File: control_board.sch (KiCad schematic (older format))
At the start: 4 parts

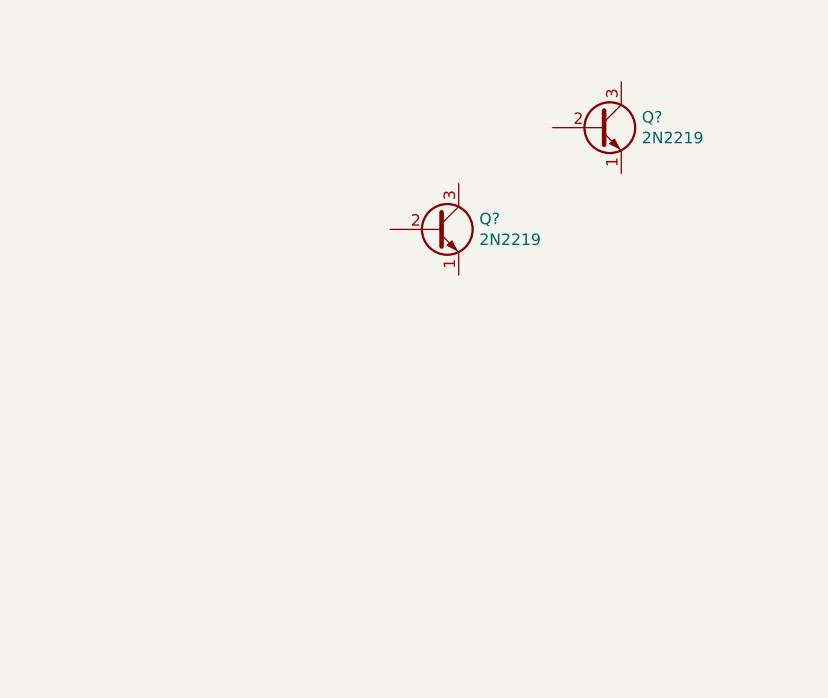
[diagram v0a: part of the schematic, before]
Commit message: Added level shifting
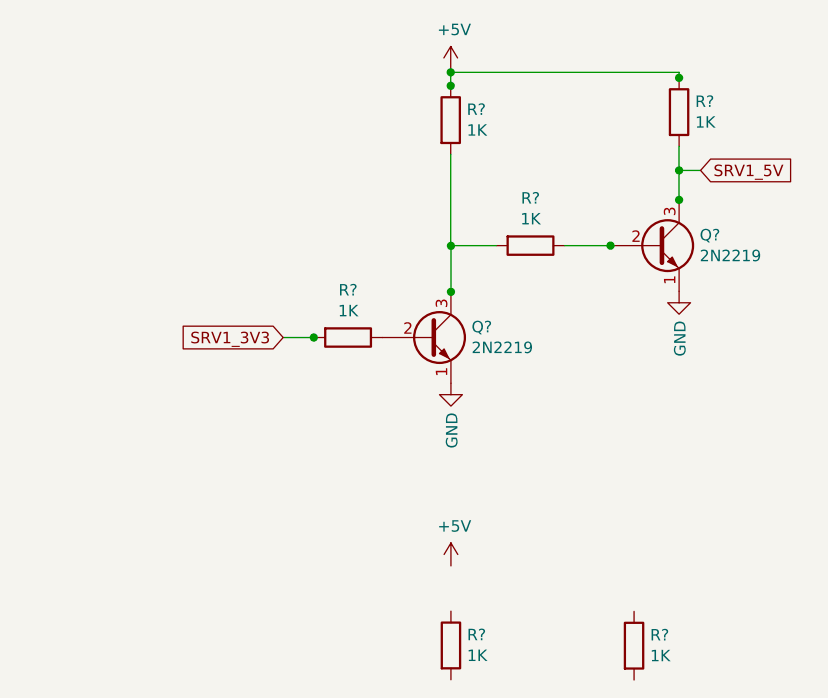
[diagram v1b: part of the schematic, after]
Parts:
- added R? (x6): 1K, symbol Device:R
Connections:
- net labels added: +5V, SRV1_3V3, SRV1_5V
- wire segments 0 -> 20
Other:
- moved on the sheet: Q?

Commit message: Routed board layout
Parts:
- added C1, C2: 10uF, Capacitor_SMD:C_0805_2012Metric, symbol Device:C
- added D1, D3, D4, D5, D6, D7, D8: LED, LED_SMD:LED_0805_2012Metric, symbol Device:LED
- added H1, H2, H3, H4, H5, H6, H7: MountingHole_Pad, MountingHole:MountingHole_3mm_Pad_Via, symbol Mechanical:MountingHole_Pad
- added J1: Conn_01x02_Female, Connector_PinHeader_2.54mm:PinHeader_1x02_P2.54mm_Vertical, symbol Connector:Conn_01x02_Female
- added J10, J15, J16: Conn_02x04_Odd_Even, Connector_PinSocket_2.54mm:PinSocket_2x04_P2.54mm_Vertical, symbol Connector_Generic:Conn_02x04_Odd_Even
- added J11: Screw_Terminal_01x02, TerminalBlock:TerminalBlock_Altech_AK300-2_P5.00mm, symbol Connector:Screw_Terminal_01x02
- added J12, J13, J14, J17, J18, J9: Conn_01x03, Connector_PinHeader_2.54mm:PinHeader_1x03_P2.54mm_Vertical, symbol Connector_Generic:Conn_01x03
- added J19: Conn_02x03_Odd_Even, Connector_PinHeader_2.54mm:PinHeader_2x03_P2.54mm_Vertical, symbol Connector_Generic:Conn_02x03_Odd_Even
- added J4, J5, J6, J7: Conn_01x01, Connector_PinSocket_2.54mm:PinSocket_1x01_P2.54mm_Vertical, symbol Connector_Generic:Conn_01x01
- added J8: Conn_01x03, Connector_PinSocket_2.54mm:PinSocket_1x03_P2.54mm_Vertical, symbol Connector_Generic:Conn_01x03
- added Q1, Q10, Q11, Q2, Q3, Q4, Q5, Q6, Q7, Q8: 2N2219, Package_TO_SOT_THT:TO-92, symbol Transistor_BJT:2N2219
- added R1, R3, R4, R5, R6, R7, R8: 220, Resistor_SMD:R_0805_2012Metric, symbol Device:R
- added R10, R11, R12, R13, R14, R16, R17, R18, R19, R20, R23, R24, R25, R26, R29, R30, R31, R32: 1K, Resistor_SMD:R_0805_2012Metric, symbol Device:R
- added R9: 1M, Resistor_SMD:R_0805_2012Metric, symbol Device:R
- added SW1, SW2, SW3, SW4: SW_Push, Button_Switch_THT:SW_PUSH_6mm, symbol Switch:SW_Push
- added TP1, TP2, TP3: TestPoint, TestPoint:TestPoint_Pad_D1.5mm, symbol Connector:TestPoint
- added U1: LM1117-3.3, Package_TO_SOT_SMD:SOT-223, symbol Regulator_Linear:LM1117-3.3
- J2, J3: renamed from J?; footprint (none) -> Connector_PinSocket_2.54mm:PinSocket_2x25_P2.54mm_Vertical
- Q12, Q9: renamed from Q?; footprint Package_TO_SOT_THT:TO-39-3 -> Package_TO_SOT_THT:TO-92
- R15, R21, R22, R27, R28, R33: renamed from R?; footprint (none) -> Resistor_SMD:R_0805_2012Metric
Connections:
- net labels added: +12V, +3.3V, DEBUG_RX, DEBUG_TX, PA_4, PD_0, PD_1, PD_2, PD_3, PD_4, PD_5, PD_6, PE_0, PE_1, PE_2, PE_3, SRV2_3V3, SRV2_5V, SRV3_3V3, SRV3_5V, SRV4_3V3, SRV4_5V, SRV5_3V3, SRV5_5V, SRV6_3V3, SRV6_5V, USART_RX, USART_TX
- wire segments 20 -> 100
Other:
- moved on the sheet: J2, J3, Q12, Q9, R15, R21, R22, R27, R28, R33

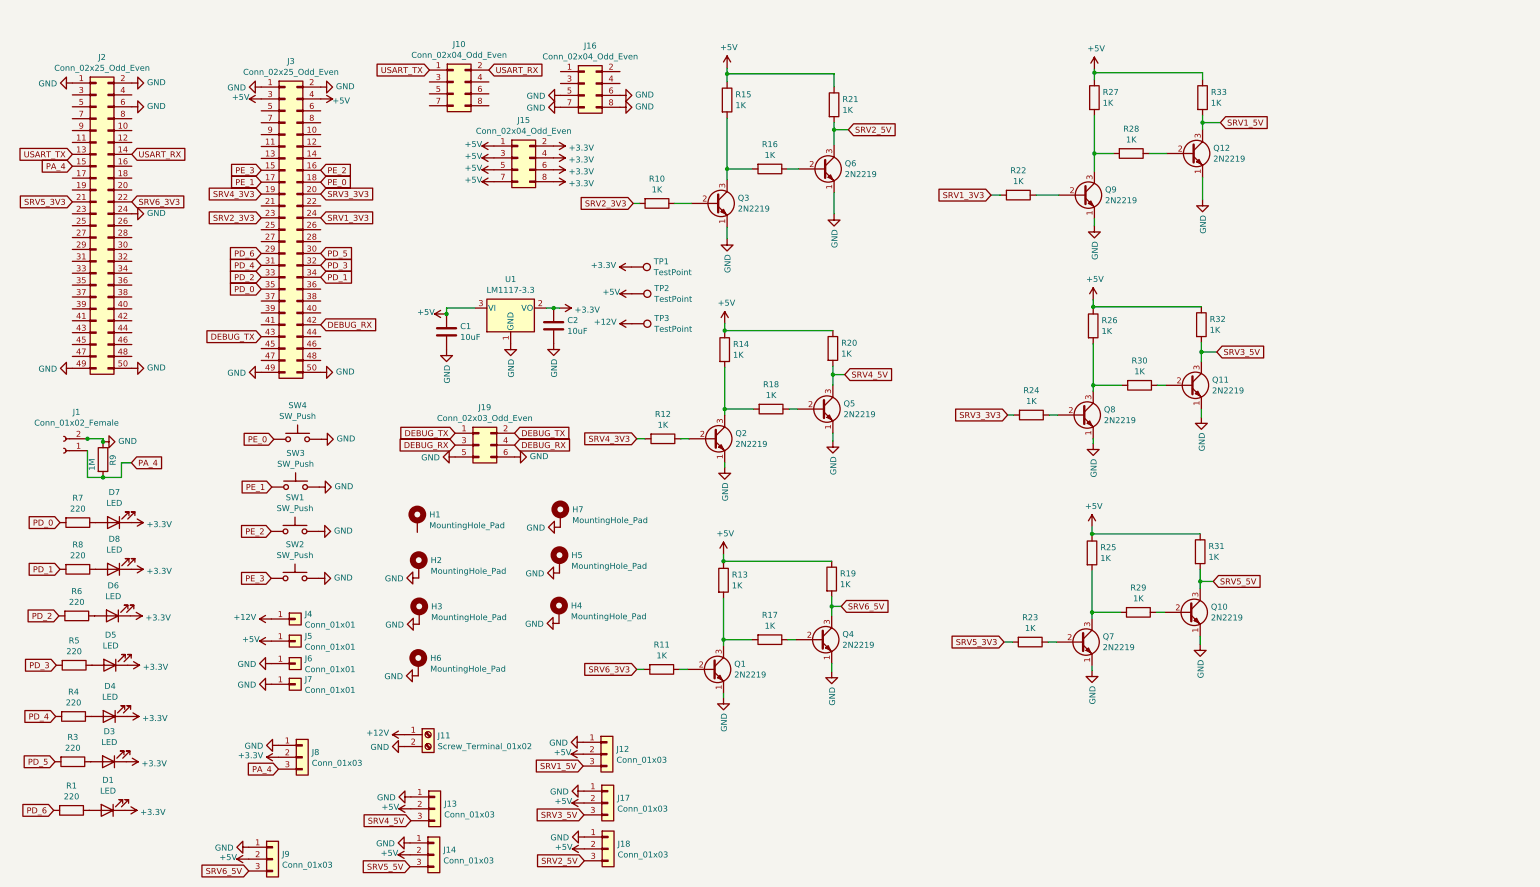
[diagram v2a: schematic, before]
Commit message: added ESP8266 circuit
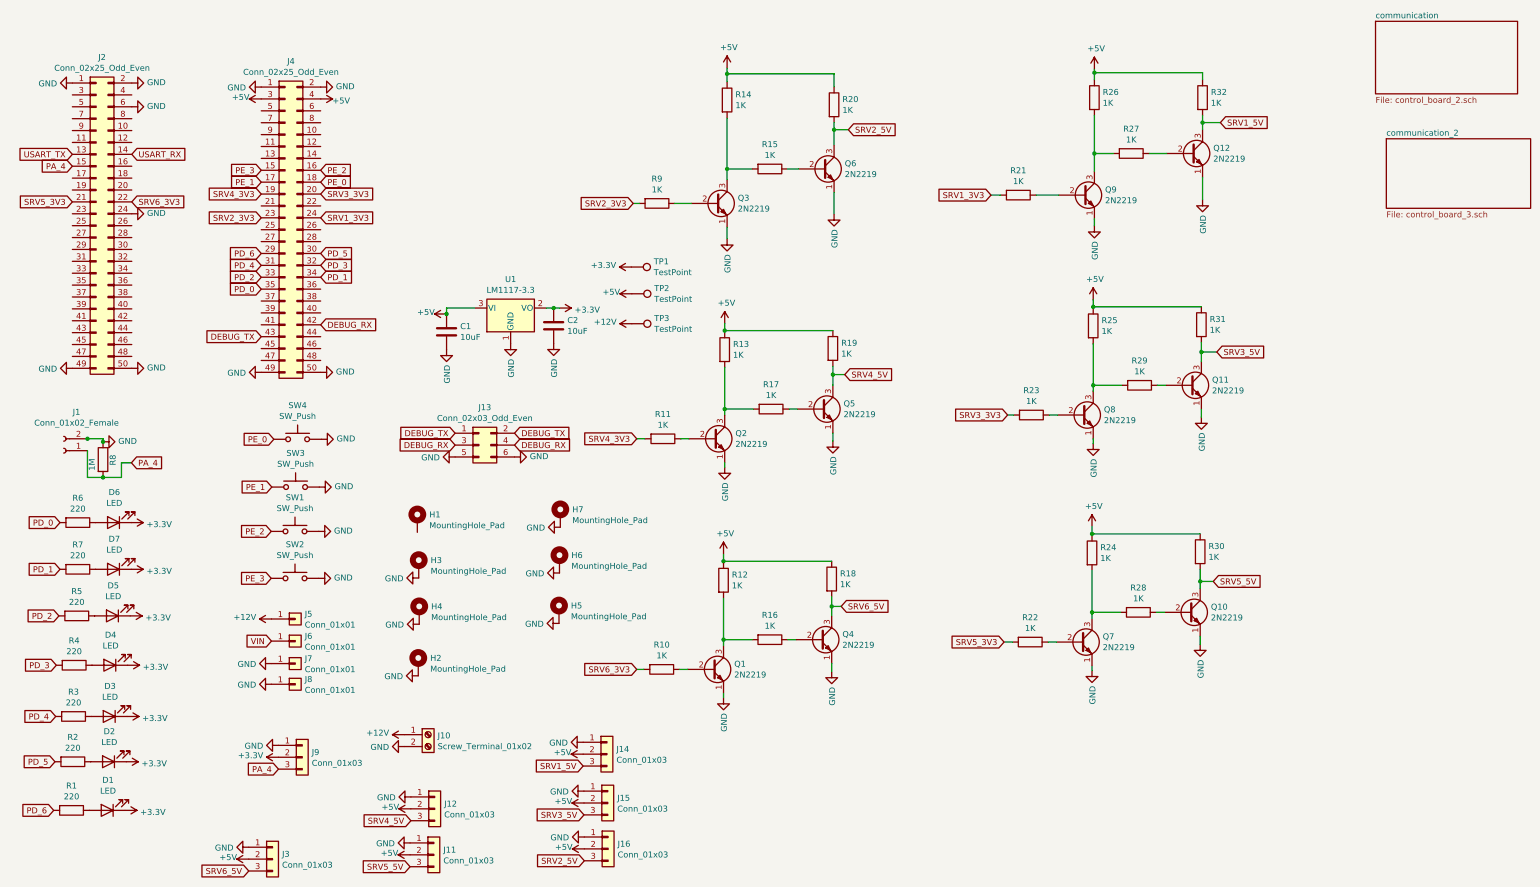
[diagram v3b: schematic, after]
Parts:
- removed J10, J15, J16: Conn_02x04_Odd_Even, Connector_PinSocket_2.54mm:PinSocket_2x04_P2.54mm_Vertical, symbol Connector_Generic:Conn_02x04_Odd_Even
- renumbered D3 to D2, D4 to D3, D5 to D4, D6 to D5, D7 to D6, D8 to D7, H6 to H2, H2 to H3, H3 to H4, H4 to H5, H5 to H6, J11 to J10, J14 to J11, J13 to J12, J19 to J13, J12 to J14, J17 to J15, J18 to J16, J9 to J3, J3 to J4, J4 to J5, J5 to J6, J6 to J7, J7 to J8, J8 to J9, R11 to R10, R12 to R11, R13 to R12, R14 to R13, R15 to R14, R16 to R15, R17 to R16, R18 to R17, R19 to R18, R20 to R19, R3 to R2, R21 to R20, R22 to R21, R23 to R22, R24 to R23, R25 to R24, R26 to R25, R27 to R26, R28 to R27, R29 to R28, R30 to R29, R4 to R3, R31 to R30, R32 to R31, R33 to R32, R5 to R4, R6 to R5, R7 to R6, R8 to R7, R9 to R8, R10 to R9
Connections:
- net +5V: no longer J6.1 (Pin_1)
- new net VIN: J6.1 (Pin_1)
